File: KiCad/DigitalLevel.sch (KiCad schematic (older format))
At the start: 67 parts, among them SW1 SW_Push_Open, SW2 SW_Push_Open, SW3 SW_Push_Open, U2 MPU-6050, U3 XC6206P332MR

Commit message: Fixed schematics
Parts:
- removed R1, R2: 10k, symbol Device:R
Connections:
- wire segments 149 -> 147
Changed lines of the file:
@@
 	1650 6450 1250 6450
-Wire Wire Line
-	1250 6450 1250 7100
-$Comp
-L Device:R R2
-U 1 1 5E2F8CA7
-P 1250 7250
-F 0 "R2" H 1320 7296 50  0000 L CNN
-F 1 "10k" H 1320 7205 50  0000 L CNN
-F 2 "" V 1180 7250 50  0001 C CNN
-F 3 "~" H 1250 7250 50  0001 C CNN
-	1    1250 7250
-	1    0    0    -1
-$EndComp
-Wire Wire Line
-	1250 7400 1250 7600
 Wire Wire Line
 	3050 6850 3350 6850
@@
 Wire Wire Line
 	1650 6750 1550 6750
-Wire Wire Line
-	1550 6750 1550 7100
-$Comp
-L Device:R R1
-U 1 1 5E2FE974
-P 1550 7250
-F 0 "R1" H 1620 7296 50  0000 L CNN
-F 1 "10k" H 1620 7205 50  0000 L CNN
-F 2 "" V 1480 7250 50  0001 C CNN
-F 3 "~" H 1550 7250 50  0001 C CNN
-	1    1550 7250
-	1    0    0    -1
-$EndComp
-Wire Wire Line
-	1550 7400 1550 7600
 $Comp
 L Device:C C1
@@
 Wire Wire Line
 	8900 5600 9500 5600
+Wire Wire Line
+	1250 6450 1250 7600
+Wire Wire Line
+	1550 6750 1550 7600
 $EndSCHEMATC

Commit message: Fixed schematics
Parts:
- removed SW1, SW2, SW3: SW_Push_Open, symbol Switch:SW_Push_Open
- added SW1, SW2, SW3: SW_Push, symbol Switch:SW_Push
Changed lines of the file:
@@
 	1    0    0    -1
-$EndComp
-$Comp
-L Switch:SW_Push_Open SW1
-U 1 1 5E5D8FE1
-P 6600 5200
-F 0 "SW1" V 6554 5277 50  0000 L CNN
-F 1 "SW_Push_Open" V 6645 5277 50  0000 L CNN
-F 2 "" H 6600 5400 50  0001 C CNN
-F 3 "~" H 6600 5400 50  0001 C CNN
-	1    6600 5200
-	0    1    1    0
 $EndComp
 Wire Wire Line
@@
 Wire Wire Line
 	6000 5600 6600 5600
-$Comp
-L Switch:SW_Push_Open SW2
-U 1 1 5EA01BE2
-P 8000 5200
-F 0 "SW2" V 7954 5277 50  0000 L CNN
-F 1 "SW_Push_Open" V 8045 5277 50  0000 L CNN
-F 2 "" H 8000 5400 50  0001 C CNN
-F 3 "~" H 8000 5400 50  0001 C CNN
-	1    8000 5200
-	0    1    1    0
-$EndComp
 Wire Wire Line
 	8000 5600 8000 5700
@@
 Wire Wire Line
 	7400 5600 8000 5600
-$Comp
-L Switch:SW_Push_Open SW3
-U 1 1 5EA07F9B
-P 9500 5200
-F 0 "SW3" V 9454 5277 50  0000 L CNN
-F 1 "SW_Push_Open" V 9545 5277 50  0000 L CNN
-F 2 "" H 9500 5400 50  0001 C CNN
-F 3 "~" H 9500 5400 50  0001 C CNN
-	1    9500 5200
-	0    1    1    0
-$EndComp
 Wire Wire Line
 	9500 5600 9500 5700
@@
 Wire Wire Line
 	1550 6750 1550 7600
+$Comp
+L Switch:SW_Push SW1
+U 1 1 5EA2ED5D
+P 6600 5200
+F 0 "SW1" V 6554 5348 50  0000 L CNN
+F 1 "SW_Push" V 6645 5348 50  0000 L CNN
+F 2 "" H 6600 5400 50  0001 C CNN
+F 3 "~" H 6600 5400 50  0001 C CNN
+	1    6600 5200
+	0    1    1    0
+$EndComp
+$Comp
+L Switch:SW_Push SW2
+U 1 1 5EA494B0
+P 8000 5200
+F 0 "SW2" V 7954 5348 50  0000 L CNN
+F 1 "SW_Push" V 8045 5348 50  0000 L CNN
+F 2 "" H 8000 5400 50  0001 C CNN
+F 3 "~" H 8000 5400 50  0001 C CNN
+	1    8000 5200
+	0    1    1    0
+$EndComp
+$Comp
+L Switch:SW_Push SW3
+U 1 1 5EA5013D
+P 9500 5200
+F 0 "SW3" V 9454 5348 50  0000 L CNN
+F 1 "SW_Push" V 9545 5348 50  0000 L CNN
+F 2 "" H 9500 5400 50  0001 C CNN
+F 3 "~" H 9500 5400 50  0001 C CNN
+	1    9500 5200
+	0    1    1    0
+$EndComp
 $EndSCHEMATC

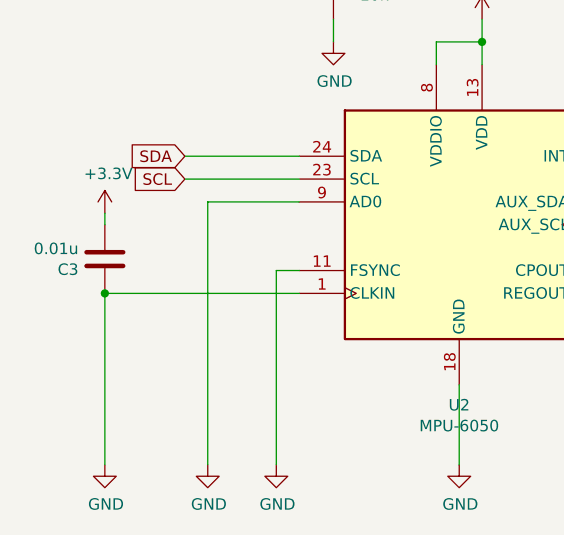
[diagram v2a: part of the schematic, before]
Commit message: Fixed schematics
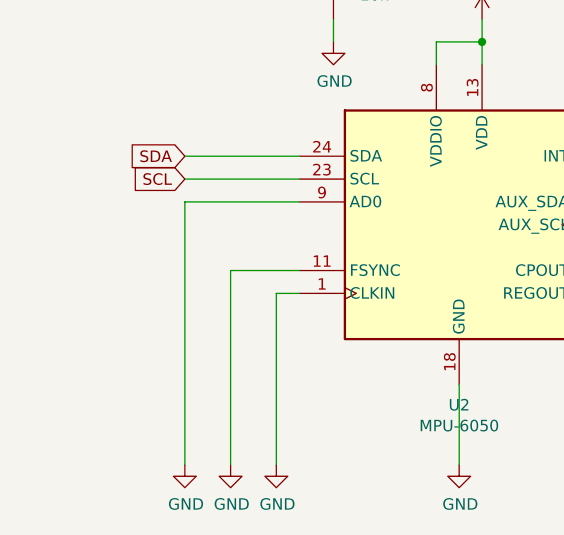
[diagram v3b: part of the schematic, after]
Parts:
- removed C3: 0.01u, symbol Device:C
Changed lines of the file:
@@
 INT
-Wire Wire Line
-	1650 6450 1250 6450
 Wire Wire Line
 	3050 6850 3350 6850
@@
 Wire Wire Line
 	3350 7400 3350 7600
-Wire Wire Line
-	1650 6750 1550 6750
 $Comp
 L Device:C C1
@@
 	2250 5850 2250 5750
 Wire Wire Line
-	800  6850 800  7600
-$Comp
-L Device:C C3
-U 1 1 5E31CE3D
-P 800 6700
-F 0 "C3" H 915 6746 50  0000 L CNN
-F 1 "0.01u" H 915 6655 50  0000 L CNN
-F 2 "" H 838 6550 50  0001 C CNN
-F 3 "~" H 800 6700 50  0001 C CNN
-	1    800  6700
-	-1   0    0    1
-$EndComp
-Wire Wire Line
-	800  6550 800  6500
-Wire Wire Line
 	1800 5750 1800 5650
 $Comp
@@
 L power:GND #PWR?
 U 1 1 5E6CB783
-P 800 7600
-F 0 "#PWR?" H 800 7350 50  0001 C CNN
-F 1 "GND" H 805 7427 50  0000 C CNN
-F 2 "" H 800 7600 50  0001 C CNN
-F 3 "" H 800 7600 50  0001 C CNN
-	1    800  7600
+P 1150 7600
+F 0 "#PWR?" H 1150 7350 50  0001 C CNN
+F 1 "GND" H 1155 7427 50  0000 C CNN
+F 2 "" H 1150 7600 50  0001 C CNN
+F 3 "" H 1150 7600 50  0001 C CNN
+	1    1150 7600
 	1    0    0    -1
 $EndComp
@@
 	1050 1850 2250 1850
 Connection ~ 2250 1850
-Connection ~ 800  6850
-Wire Wire Line
-	800  6850 1650 6850
 $Comp
 L power:GND #PWR?
 U 1 1 5E9579DB
-P 1250 7600
-F 0 "#PWR?" H 1250 7350 50  0001 C CNN
-F 1 "GND" H 1255 7427 50  0000 C CNN
-F 2 "" H 1250 7600 50  0001 C CNN
-F 3 "" H 1250 7600 50  0001 C CNN
-	1    1250 7600
+P 1350 7600
+F 0 "#PWR?" H 1350 7350 50  0001 C CNN
+F 1 "GND" H 1355 7427 50  0000 C CNN
+F 2 "" H 1350 7600 50  0001 C CNN
+F 3 "" H 1350 7600 50  0001 C CNN
+	1    1350 7600
 	1    0    0    -1
 $EndComp
@@
 $Comp
 L power:+3.3V #PWR?
-U 1 1 5E9A73F6
-P 800 6500
-F 0 "#PWR?" H 800 6350 50  0001 C CNN
-F 1 "+3.3V" H 815 6673 50  0000 C CNN
-F 2 "" H 800 6500 50  0001 C CNN
-F 3 "" H 800 6500 50  0001 C CNN
-	1    800  6500
-	1    0    0    -1
-$EndComp
-$Comp
-L power:+3.3V #PWR?
 U 1 1 5E9ADF66
 P 2450 5650
@@
 Wire Wire Line
 	8900 5600 9500 5600
-Wire Wire Line
-	1250 6450 1250 7600
-Wire Wire Line
-	1550 6750 1550 7600
 $Comp
 L Switch:SW_Push SW1
@@
 	0    1    1    0
 $EndComp
+Wire Wire Line
+	1150 6450 1150 7600
+Wire Wire Line
+	1350 7600 1350 6750
+Wire Wire Line
+	1650 6850 1550 6850
+Wire Wire Line
+	1550 6850 1550 7600
+Wire Wire Line
+	1350 6750 1650 6750
+Wire Wire Line
+	1150 6450 1650 6450
 $EndSCHEMATC

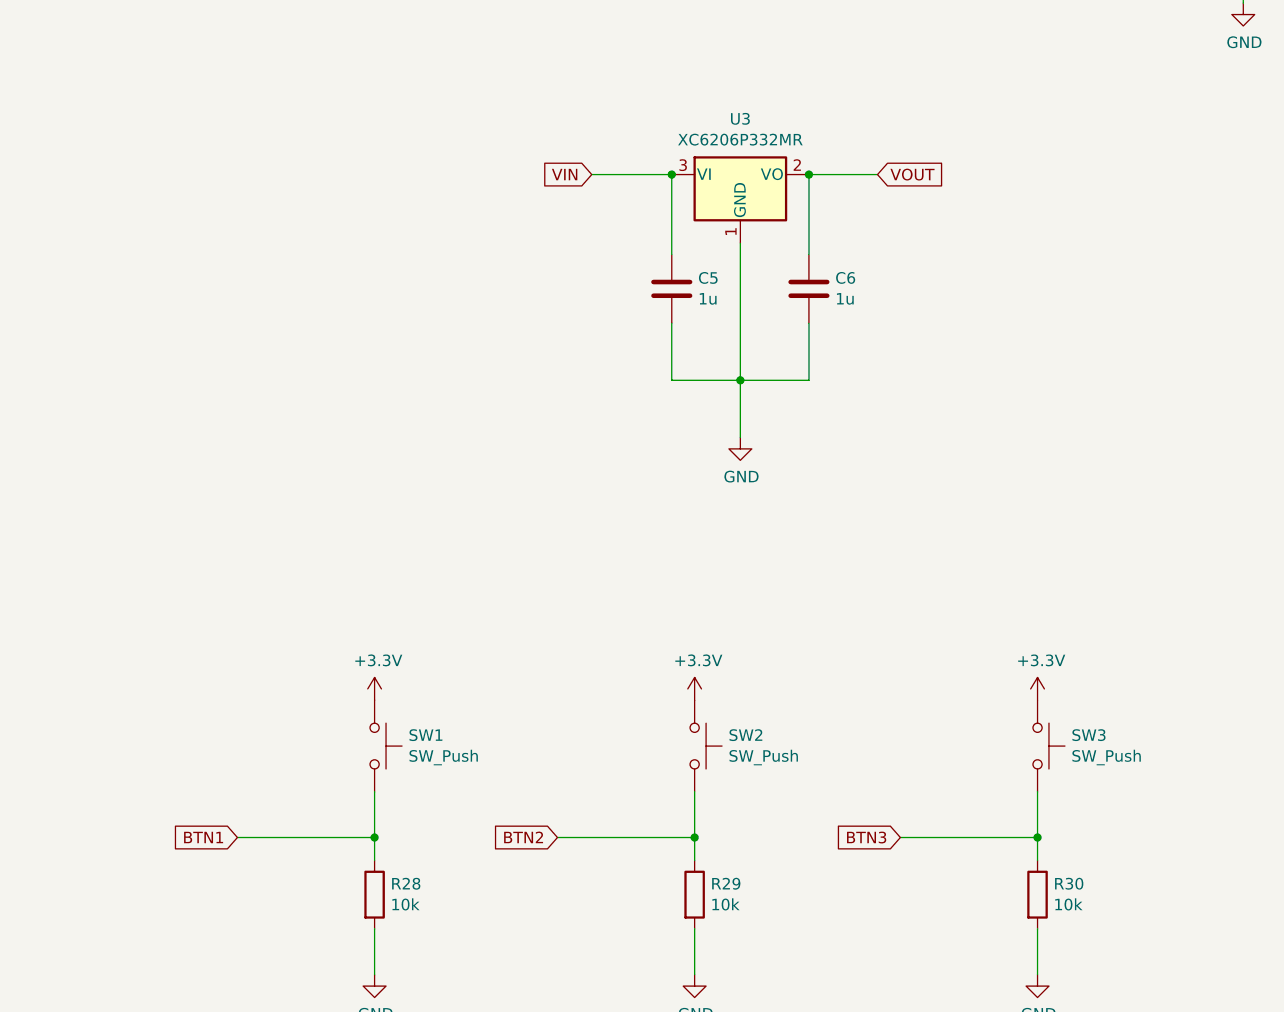
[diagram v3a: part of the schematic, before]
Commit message: Fixed schematics
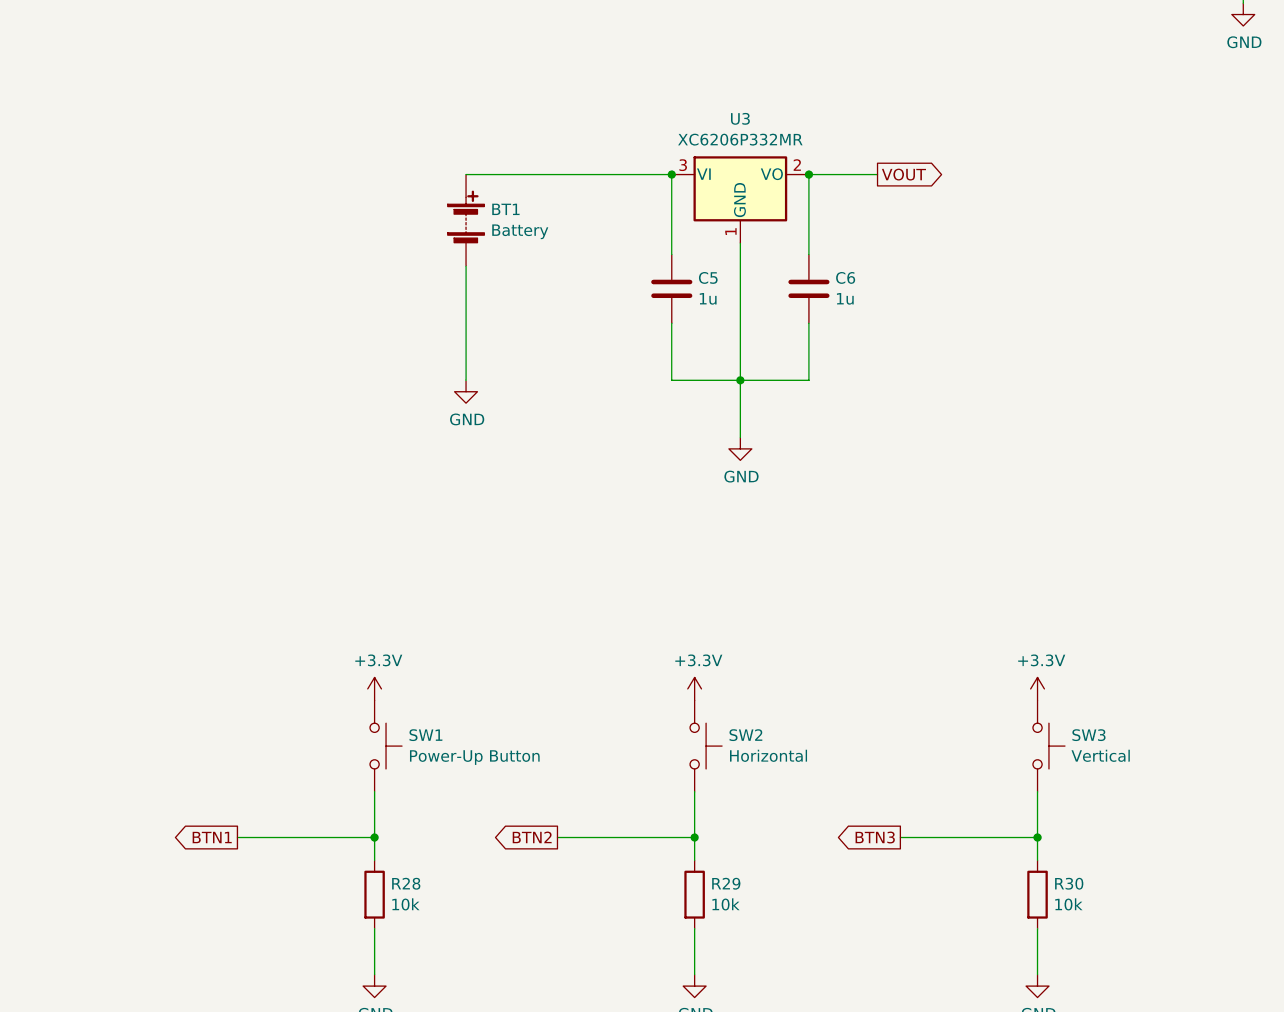
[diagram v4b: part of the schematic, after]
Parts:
- added BT1: Battery, symbol Device:Battery
- SW1: value SW_Push -> Power-Up Button
- SW2: value SW_Push -> Horizontal
- SW3: value SW_Push -> Vertical
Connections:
- net GND: now also BT1.2 (-)
- net VIN: no longer names the net of C5.1, U3.3 (VI)
- net VIN: now also BT1.1 (+)
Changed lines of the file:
@@
 Wire Wire Line
 	2350 7250 2350 7600
-Text GLabel 7550 2700 0    50   Input ~ 0
-VIN
-Text GLabel 8800 2700 2    50   Input ~ 0
+Text GLabel 8800 2700 2    50   Output ~ 0
 VOUT
 $Comp
@@
 Wire Wire Line
 	6600 6000 6600 6200
-Text GLabel 6000 5600 0    50   Input ~ 0
+Text GLabel 6000 5600 0    50   Output ~ 0
 BTN1
 $Comp
@@
 Wire Wire Line
 	7900 3600 8200 3600
-Wire Wire Line
-	7550 2700 7900 2700
 Connection ~ 7900 2700
 Connection ~ 8500 2700
@@
 Wire Wire Line
 	8000 6000 8000 6200
-Text GLabel 7400 5600 0    50   Input ~ 0
+Text GLabel 7400 5600 0    50   Output ~ 0
 BTN2
 $Comp
@@
 Wire Wire Line
 	9500 6000 9500 6200
-Text GLabel 8900 5600 0    50   Input ~ 0
+Text GLabel 8900 5600 0    50   Output ~ 0
 BTN3
 $Comp
@@
 P 6600 5200
 F 0 "SW1" V 6554 5348 50  0000 L CNN
-F 1 "SW_Push" V 6645 5348 50  0000 L CNN
+F 1 "Power-Up Button" V 6645 5348 50  0000 L CNN
 F 2 "" H 6600 5400 50  0001 C CNN
 F 3 "~" H 6600 5400 50  0001 C CNN
@@
 P 8000 5200
 F 0 "SW2" V 7954 5348 50  0000 L CNN
-F 1 "SW_Push" V 8045 5348 50  0000 L CNN
+F 1 "Horizontal" V 8045 5348 50  0000 L CNN
 F 2 "" H 8000 5400 50  0001 C CNN
 F 3 "~" H 8000 5400 50  0001 C CNN
@@
 P 9500 5200
 F 0 "SW3" V 9454 5348 50  0000 L CNN
-F 1 "SW_Push" V 9545 5348 50  0000 L CNN
+F 1 "Vertical" V 9545 5348 50  0000 L CNN
 F 2 "" H 9500 5400 50  0001 C CNN
 F 3 "~" H 9500 5400 50  0001 C CNN
@@
 Wire Wire Line
 	1150 6450 1650 6450
+$Comp
+L Device:Battery BT1
+U 1 1 5EAA7AF4
+P 7000 2900
+F 0 "BT1" H 7108 2946 50  0000 L CNN
+F 1 "Battery" H 7108 2855 50  0000 L CNN
+F 2 "" V 7000 2960 50  0001 C CNN
+F 3 "~" V 7000 2960 50  0001 C CNN
+	1    7000 2900
+	1    0    0    -1
+$EndComp
+Wire Wire Line
+	7000 2700 7900 2700
+Wire Wire Line
+	7000 3100 7000 3600
+$Comp
+L power:GND #PWR?
+U 1 1 5EABCA3C
+P 7000 3600
+F 0 "#PWR?" H 7000 3350 50  0001 C CNN
+F 1 "GND" H 7005 3427 50  0000 C CNN
+F 2 "" H 7000 3600 50  0001 C CNN
+F 3 "" H 7000 3600 50  0001 C CNN
+	1    7000 3600
+	1    0    0    -1
+$EndComp
 $EndSCHEMATC

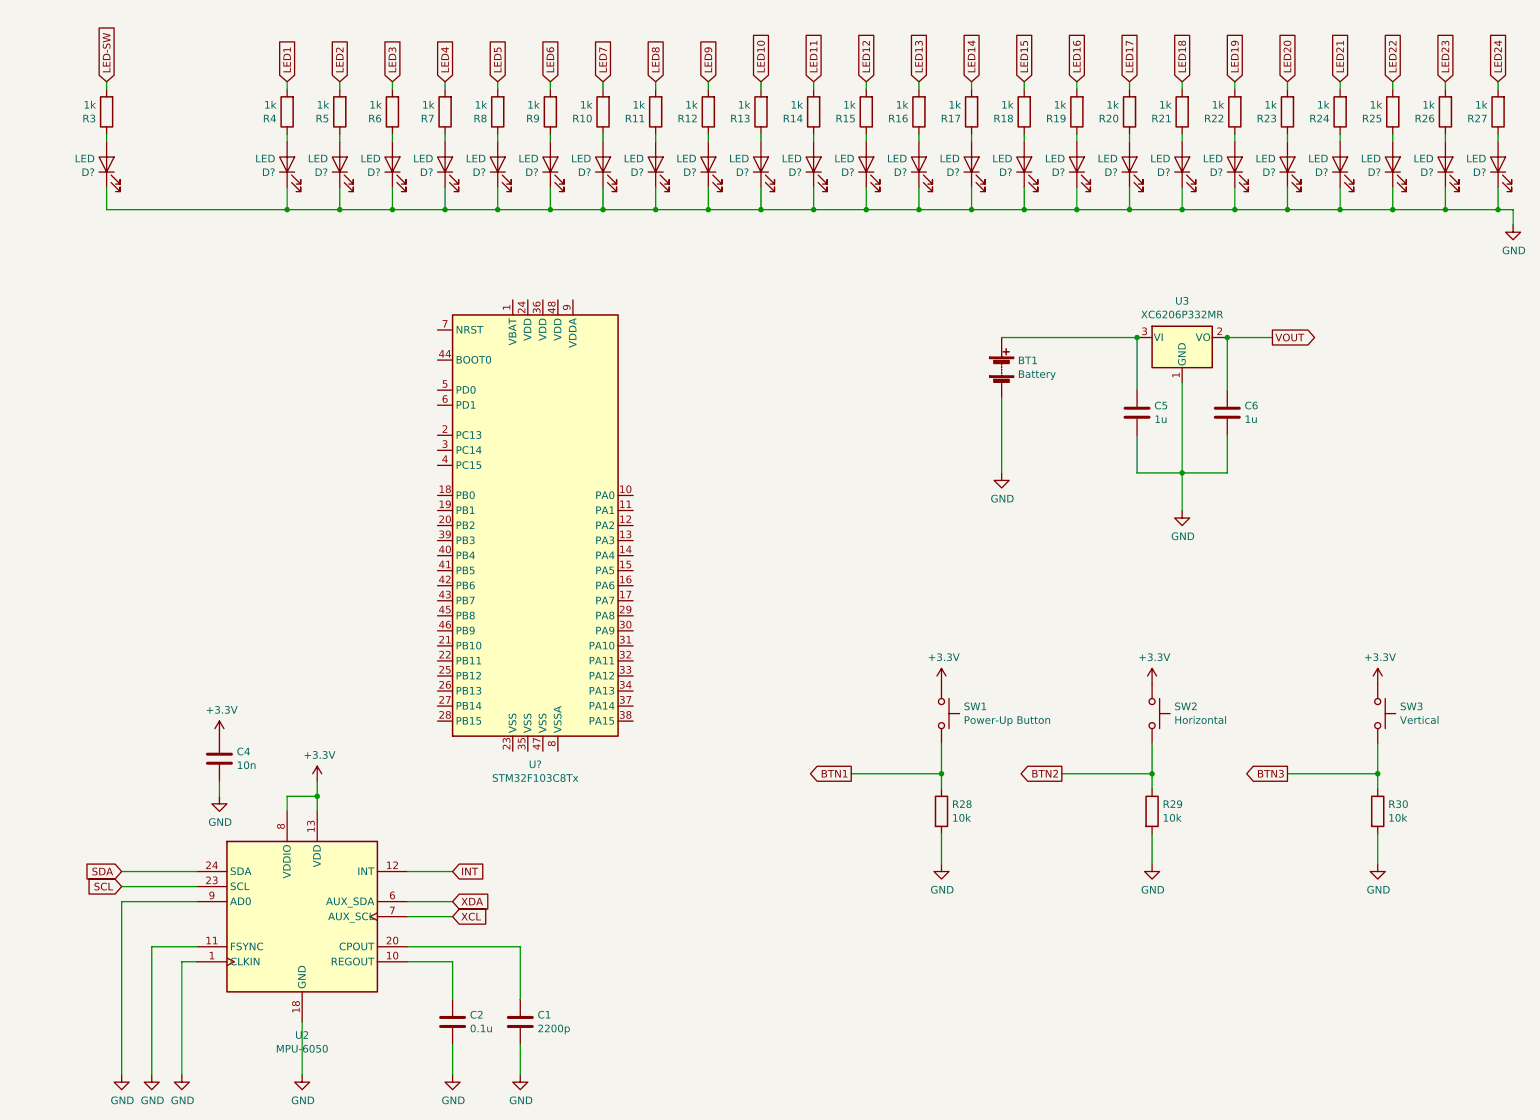
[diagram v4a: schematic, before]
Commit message: Fixed schematics
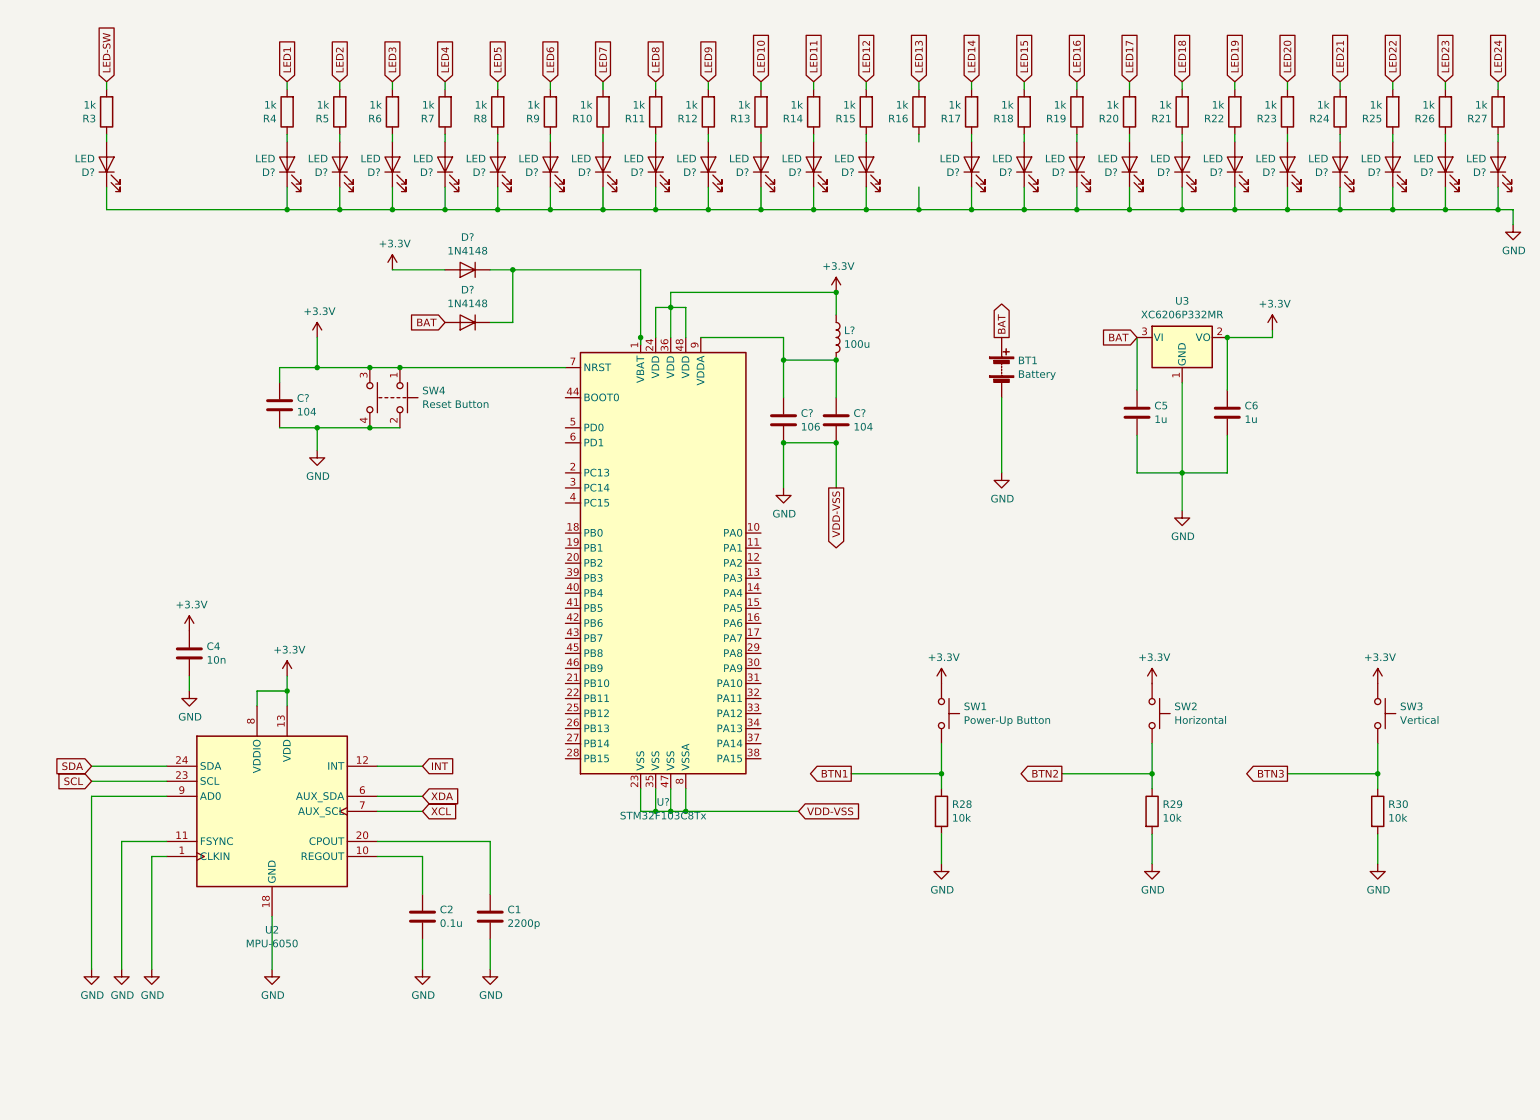
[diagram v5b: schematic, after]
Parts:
- removed D?: LED, symbol Device:LED
- added C? (x2): 104, symbol Device:C
- added C?: 106, symbol Device:C
- added D? (x2): 1N4148, Diode_THT:D_DO-35_SOD27_P7.62mm_Horizontal, symbol Diode:1N4148
- added L?: 100u, symbol Device:L
- added SW4: Reset Button, symbol Switch:SW_Push_Dual
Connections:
- net VOUT is gone; now on net +3V3: C6.1, U3.2 (VO)
- net +3V3: now also U?.24 (VDD), U?.36 (VDD), U?.48 (VDD), U?.7 (NRST), C?.1, D?.2 (A), L?.1, SW4.1, SW4.3
- net GND: now also U?.23 (VSS), U?.35 (VSS), U?.47 (VSS), U?.8 (VSSA), C?.2, C?.2, C?.2, SW4.2, SW4.4
- net BAT: now reaches BT1.1 (+), C5.1, U3.3 (VI)
- net BAT: now also D?.2 (A)
- net at U?.1 (VBAT): now also D?.1 (K), D?.1 (K)
- net at U?.9 (VDDA): now also C?.1, C?.1, L?.2
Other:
- moved on the sheet: C1, C2, C4, U2, U?
